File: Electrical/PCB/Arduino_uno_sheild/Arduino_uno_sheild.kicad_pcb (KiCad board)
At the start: 2 copper layers, 68.6 x 53.3 mm, 15 parts, among them J1 ED10523-ND, J2 6posheader, J3 6posheader, J4 6posheader, J5 6posheader, J6 ED2580-ND

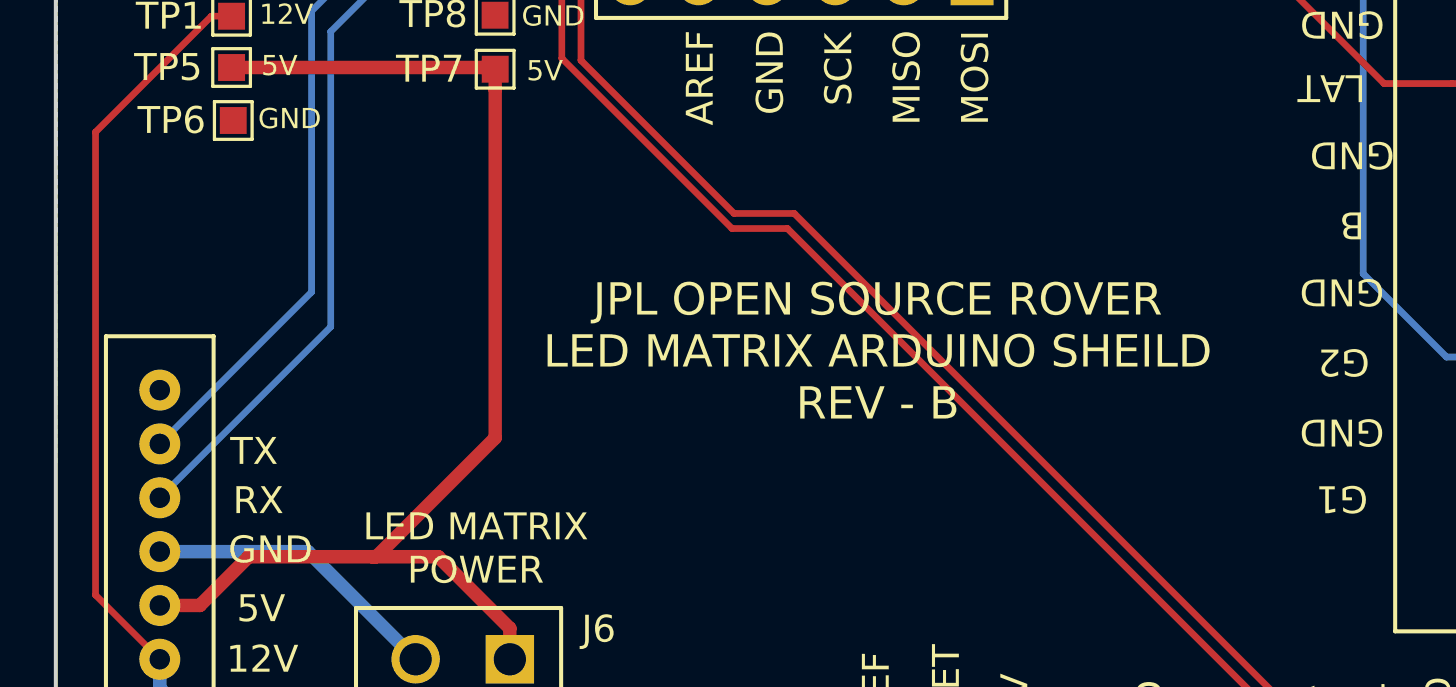
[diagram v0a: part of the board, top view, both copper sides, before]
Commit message: Adding board Rev-E of control board with updated silkscreen images, and Rev-D of arduino board also with silk screen fixes
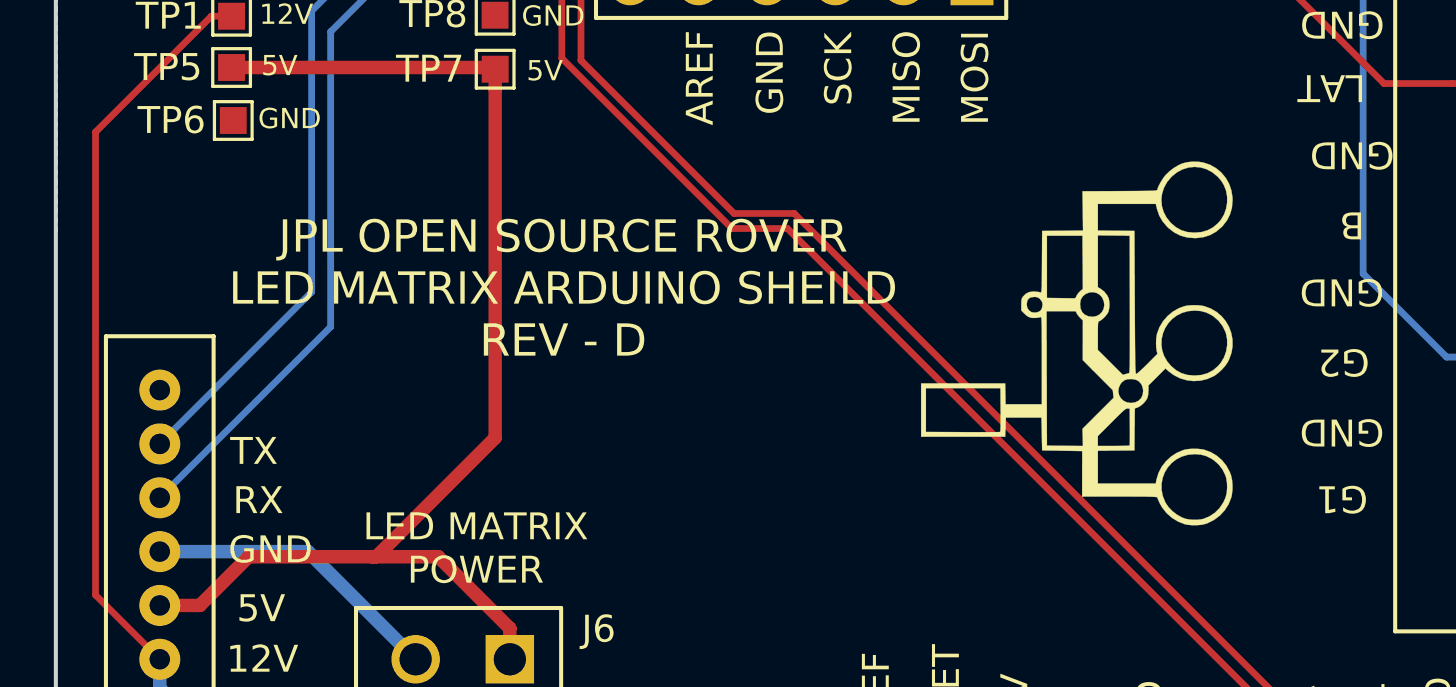
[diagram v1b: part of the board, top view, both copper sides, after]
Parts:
- added y1: rover_silkscreen, JPL Robotics:rover_image, F.Cu at (38.5, -27.7)
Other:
- board text added: "JPL OPEN SOURCE ROVER LED MATRIX ARDUINO SHEILD REV - D"
- board text removed: "JPL OPEN SOURCE ROVER LED MATRIX ARDUINO SHEILD REV - B"
